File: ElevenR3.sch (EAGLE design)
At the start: 63 parts, among them IC1 ATMEGA328P, IC2 ATMEGA8U2-MU, IC3 MC33269DT-5.0, IC4 LM358D, IC5 LP2985-33DBVR, J2 Analog, J3 Digital_8_13, J4 Digital_0_7, J5 DC_2_1MM, J6 Digital_0_7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

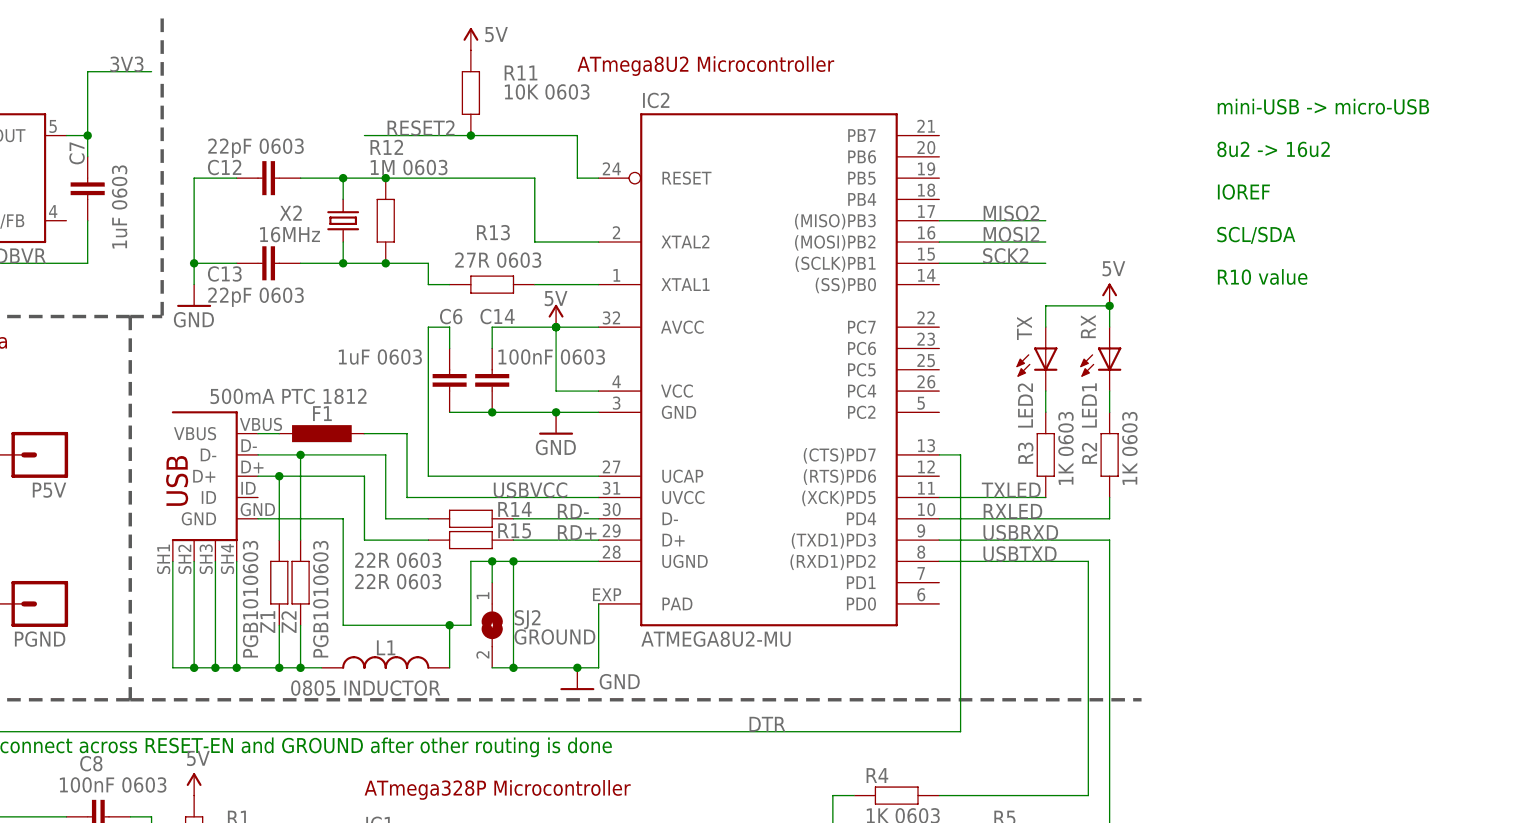
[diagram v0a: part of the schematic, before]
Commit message: Routed I2C and converted to microUSB
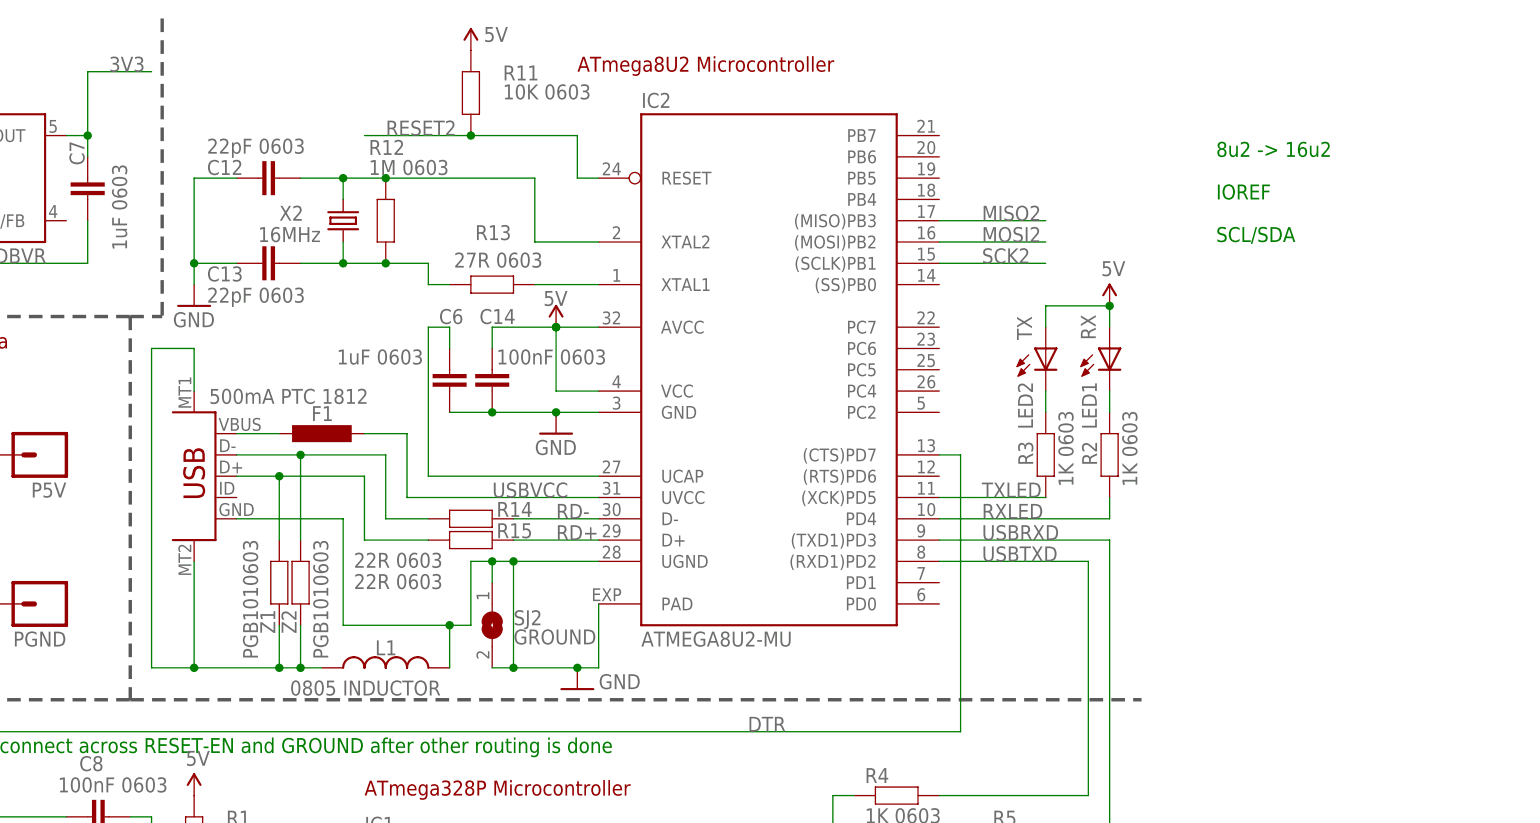
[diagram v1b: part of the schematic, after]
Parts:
- removed P1: USB-FT, freetronics-master-v1:USB-FT
- added X3: USBSF-MICROB, freetronics-jon:USBSF-MICROB
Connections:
- net GND: now also X3.GND; no longer P1.GND
- net N$115: now also X3.VBUS; no longer P1.VBUS
- net N$16: now also X3.D+; no longer P1.D+
- net N$17: now also X3.D-; no longer P1.D-
- net N$3: now also X3.MT1, X3.MT2; no longer P1.SH$1, P1.SH$2, P1.SH$3, P1.SH$4
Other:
- note removed: "R10 value"
- note removed: "mini-USB -> micro-USB"
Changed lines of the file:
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@@
 <layer number="101" name="Patch_Top" color="12" fill="4" visible="yes" active="yes"/>
 <layer number="102" name="Vscore" color="7" fill="1" visible="yes" active="yes"/>
+<layer number="103" name="fp3" color="7" fill="1" visible="yes" active="yes"/>
 <layer number="104" name="Name" color="7" fill="1" visible="yes" active="yes"/>
+<layer number="105" name="Beschreib" color="9" fill="1" visible="yes" active="yes"/>
+<layer number="106" name="BGA-Top" color="4" fill="1" visible="yes" active="yes"/>
+<layer number="107" name="BD-Top" color="5" fill="1" visible="yes" active="yes"/>
+<layer number="108" name="fp8" color="7" fill="1" visible="yes" active="yes"/>
+<layer number="109" name="fp9" color="7" fill="1" visible="yes" active="yes"/>
+<layer number="110" name="fp0" color="7" fill="1" visible="yes" active="yes"/>
+<layer number="111" name="LPC17xx" color="7" fill="1" visible="yes" active="yes"/>
+<layer number="112" name="tSilk" color="7" fill="1" visible="yes" active="yes"/>
 <layer number="116" name="Patch_BOT" color="9" fill="4" visible="yes" active="yes"/>
 <layer number="121" name="_tsilk" color="7" fill="1" visible="yes" active="yes"/>
 <layer number="122" name="_bsilk" color="7" fill="1" visible="yes" active="yes"/>
+<layer number="123" name="tTestmark" color="7" fill="1" visible="yes" active="yes"/>
+<layer number="124" name="bTestmark" color="7" fill="1" visible="yes" active="yes"/>
+<layer number="125" name="_tNames" color="7" fill="1" visible="yes" active="yes"/>
+<layer number="126" name="_bNames" color="7" fill="1" visible="yes" active="yes"/>
+<layer number="127" name="_tValues" color="7" fill="1" visible="yes" active="yes"/>
+<layer number="128" name="_bValues" color="7" fill="1" visible="yes" active="yes"/>
+<layer number="131" name="tAdjust" color="7" fill="1" visible="yes" active="yes"/>
+<layer number="132" name="bAdjust" color="7" fill="1" visible="yes" active="yes"/>
+<layer number="144" name="Drill_legend" color="7" fill="1" visible="yes" active="yes"/>
 <layer number="151" name="HeatSink" color="7" fill="1" visible="yes" active="yes"/>
+<layer number="152" name="_bDocu" color="7" fill="1" visible="yes" active="yes"/>
+<layer number="199" name="Contour" color="7" fill="1" visible="yes" active="yes"/>
 <layer number="200" name="200bmp" color="1" fill="10" visible="no" active="no"/>
 <layer number="201" name="201bmp" color="2" fill="1" visible="no" active="no"/>
@@
 <layer number="223" name="223bmp" color="7" fill="1" visible="yes" active="yes"/>
 <layer number="224" name="224bmp" color="7" fill="1" visible="yes" active="yes"/>
+<layer number="231" name="Eagle3D_PG1" color="7" fill="1" visible="yes" active="yes"/>
+<layer number="232" name="Eagle3D_PG2" color="7" fill="1" visible="yes" active="yes"/>
+<layer number="233" name="Eagle3D_PG3" color="7" fill="1" visible="yes" active="yes"/>
+<layer number="248" name="Housing" color="7" fill="1" visible="yes" active="yes"/>
+<layer number="249" name="Edge" color="7" fill="1" visible="yes" active="yes"/>
 <layer number="250" name="Descript" color="3" fill="1" visible="no" active="no"/>
 <layer number="251" name="SMDround" color="12" fill="11" visible="no" active="no"/>
@@
 <part name="L1" library="freetronics-master-v1" deviceset="INDUCTOR" device="0805-LARGE" value="0805 INDUCTOR"/>
 <part name="C6" library="freetronics" deviceset="CAP" device="0603" value="1uF 0603"/>
-<part name="P1" library="freetronics-master-v1" deviceset="USB-FT" device=""/>
 <part name="GND1" library="SparkFun" deviceset="GND" device=""/>
 <part name="GND6" library="SparkFun" deviceset="GND" device=""/>
 <part name="J6" library="freetronics" deviceset="M08" device="" value="Digital_0_7"/>
+<part name="X3" library="freetronics-jon" deviceset="USBSF" device="-MICROB"/>
 </parts>
 <sheets>
@@
 <frame x1="210.82" y1="5.08" x2="243.84" y2="10.16" columns="8" rows="5" layer="94"/>
 <frame x1="88.9" y1="101.6" x2="121.92" y2="139.7" columns="0" rows="0" layer="94"/>
-<text x="254" y="170.18" size="1.778" layer="91">mini-USB -&gt; micro-USB</text>
 <text x="254" y="165.1" size="1.778" layer="91">8u2 -&gt; 16u2</text>
 <text x="254" y="160.02" size="1.778" layer="91">IOREF</text>
 <text x="254" y="154.94" size="1.778" layer="91">SCL/SDA</text>
-<text x="254" y="149.86" size="1.778" layer="91">R10 value</text>
 </plain>
 <instances>
@@
 <attribute name="VALUE" x="149.098" y="140.335" size="1.778" layer="96"/>
 </instance>
-<instance part="P1" gate="G$1" x="127" y="121.92"/>
 <instance part="GND1" gate="1" x="175.26" y="132.08"/>
 <instance part="GND6" gate="1" x="177.8" y="101.6" smashed="yes">
@@
 <attribute name="VALUE" x="8.128" y="31.75" size="1.778" layer="96" rot="MR180"/>
 </instance>
+<instance part="X3" gate="G$1" x="132.08" y="127" rot="R180"/>
 </instances>
 <busses>
@@
 <wire x1="170.18" y1="104.14" x2="177.8" y2="104.14" width="0.1524" layer="91"/>
 <wire x1="170.18" y1="104.14" x2="170.18" y2="116.84" width="0.1524" layer="91"/>
-<wire x1="139.7" y1="121.92" x2="149.86" y2="121.92" width="0.1524" layer="91"/>
+<wire x1="137.16" y1="121.92" x2="149.86" y2="121.92" width="0.1524" layer="91"/>
 <wire x1="149.86" y1="121.92" x2="149.86" y2="109.22" width="0.1524" layer="91"/>
 <wire x1="149.86" y1="109.22" x2="162.56" y2="109.22" width="0.1524" layer="91"/>
@@
 <pinref part="GND6" gate="1" pin="GND"/>
 <pinref part="SJ2" gate="1" pin="2"/>
-<pinref part="P1" gate="G$1" pin="GND"/>
 <pinref part="L1" gate="G$1" pin="2"/>
 <pinref part="IC2" gate="G$1" pin="UGND"/>
 <pinref part="SJ2" gate="1" pin="1"/>
+<pinref part="X3" gate="G$1" pin="GND"/>
 </segment>
 </net>
@@
 <net name="N$3" class="0">
 <segment>
-<wire x1="129.54" y1="116.84" x2="129.54" y2="104.14" width="0.1524" layer="91"/>
-<wire x1="129.54" y1="104.14" x2="132.08" y2="104.14" width="0.1524" layer="91"/>
-<wire x1="132.08" y1="104.14" x2="134.62" y2="104.14" width="0.1524" layer="91"/>
-<wire x1="134.62" y1="104.14" x2="137.16" y2="104.14" width="0.1524" layer="91"/>
-<wire x1="137.16" y1="104.14" x2="142.24" y2="104.14" width="0.1524" layer="91"/>
 <wire x1="142.24" y1="104.14" x2="144.78" y2="104.14" width="0.1524" layer="91"/>
-<wire x1="132.08" y1="116.84" x2="132.08" y2="104.14" width="0.1524" layer="91"/>
-<wire x1="134.62" y1="116.84" x2="134.62" y2="104.14" width="0.1524" layer="91"/>
-<wire x1="137.16" y1="116.84" x2="137.16" y2="104.14" width="0.1524" layer="91"/>
 <wire x1="142.24" y1="109.22" x2="142.24" y2="104.14" width="0.1524" layer="91"/>
 <wire x1="144.78" y1="109.22" x2="144.78" y2="104.14" width="0.1524" layer="91"/>
 <wire x1="144.78" y1="104.14" x2="147.32" y2="104.14" width="0.1524" layer="91"/>
-<junction x="132.08" y="104.14"/>
-<junction x="134.62" y="104.14"/>
-<junction x="137.16" y="104.14"/>
 <junction x="142.24" y="104.14"/>
 <junction x="144.78" y="104.14"/>
-<pinref part="P1" gate="G$1" pin="SH$1"/>
-<pinref part="P1" gate="G$1" pin="SH$2"/>
-<pinref part="P1" gate="G$1" pin="SH$3"/>
-<pinref part="P1" gate="G$1" pin="SH$4"/>
 <pinref part="Z1" gate="G$1" pin="2"/>
 <pinref part="Z2" gate="G$1" pin="2"/>
 <pinref part="L1" gate="G$1" pin="1"/>
+<pinref part="X3" gate="G$1" pin="MT2"/>
+<wire x1="132.08" y1="116.84" x2="132.08" y2="104.14" width="0.1524" layer="91"/>
+<wire x1="132.08" y1="104.14" x2="142.24" y2="104.14" width="0.1524" layer="91"/>
+<pinref part="X3" gate="G$1" pin="MT1"/>
+<wire x1="132.08" y1="137.16" x2="132.08" y2="142.24" width="0.1524" layer="91"/>
+<wire x1="132.08" y1="142.24" x2="127" y2="142.24" width="0.1524" layer="91"/>
+<wire x1="127" y1="142.24" x2="127" y2="104.14" width="0.1524" layer="91"/>
+<wire x1="127" y1="104.14" x2="132.08" y2="104.14" width="0.1524" layer="91"/>
+<junction x="132.08" y="104.14"/>
 </segment>
 </net>
@@
 <segment>
 <wire x1="142.24" y1="119.38" x2="142.24" y2="127" width="0.1524" layer="91"/>
-<wire x1="142.24" y1="127" x2="139.7" y2="127" width="0.1524" layer="91"/>
 <wire x1="142.24" y1="127" x2="152.4" y2="127" width="0.1524" layer="91"/>
 <wire x1="152.4" y1="127" x2="152.4" y2="119.38" width="0.1524" layer="91"/>
@@
 <junction x="142.24" y="127"/>
 <pinref part="Z1" gate="G$1" pin="1"/>
-<pinref part="P1" gate="G$1" pin="D+"/>
 <pinref part="R15" gate="G$1" pin="2"/>
+<pinref part="X3" gate="G$1" pin="D+"/>
+<wire x1="142.24" y1="127" x2="137.16" y2="127" width="0.1524" layer="91"/>
 </segment>
 </net>
@@
 <segment>
 <wire x1="144.78" y1="119.38" x2="144.78" y2="129.54" width="0.1524" layer="91"/>
-<wire x1="144.78" y1="129.54" x2="139.7" y2="129.54" width="0.1524" layer="91"/>
 <wire x1="160.02" y1="121.92" x2="154.94" y2="121.92" width="0.1524" layer="91"/>
 <wire x1="154.94" y1="121.92" x2="154.94" y2="129.54" width="0.1524" layer="91"/>
@@
 <junction x="144.78" y="129.54"/>
 <pinref part="Z2" gate="G$1" pin="1"/>
-<pinref part="P1" gate="G$1" pin="D-"/>
 <pinref part="R14" gate="G$1" pin="2"/>
+<pinref part="X3" gate="G$1" pin="D-"/>
+<wire x1="137.16" y1="129.54" x2="144.78" y2="129.54" width="0.1524" layer="91"/>
 </segment>
 </net>
 <net name="N$115" class="0">
 <segment>
-<wire x1="142.24" y1="132.08" x2="139.7" y2="132.08" width="0.1524" layer="91"/>
 <pinref part="F1" gate="G$1" pin="1"/>
-<pinref part="P1" gate="G$1" pin="VBUS"/>
-</segment>
-</net>
+<pinref part="X3" gate="G$1" pin="VBUS"/>
+<wire x1="142.24" y1="132.08" x2="137.16" y2="132.08" width="0.1524" layer="91"/>
+</segment>
+</net>

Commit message: Overlay, layout, and schematic tweaks
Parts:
- IC2: value ATMEGA8U2-MU -> ATMEGA16U2-MU
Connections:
- new net N$1: C8.1, SJ1.2
- new net N$116: IC2.UGND, L1.2, SJ2.1, X3.GND
- net DTR: no longer C8.1, SJ1.2
- net GND: no longer IC2.UGND, L1.2, SJ2.1, X3.GND
- net N$3: now also X3.FIX1, X3.FIX2, X3.TAB1, X3.TAB2; no longer X3.MT1, X3.MT2
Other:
- note added: "(C)2012 Freetronics Pty Ltd: www.freetronics.com"
- note added: "(Linked)"
- note added: "Freetronics "Eleven" R3"
- note added: "Released under the TAPR Open Hardware License: www.tapr.org/ohl"
- note added: "V3.0 (2012-07-02)"
- note added: "www.freetronics.com/eleven"
- note removed: "8u2 -> 16u2"
- note removed: "Arduino Compatible Board"
- note removed: "Freetronics Eleven"
- note removed: "Version 1.0"
- note removed: "www.freetronics.com"
- moved on the sheet: C11, IC1, IC4A, IC4B, LED3, P5V, PGND, Q1, Q2, R4, R5, R7

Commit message: Clearances
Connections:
- net N$116 renamed UGND
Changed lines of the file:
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@@
 </segment>
 </net>
-<net name="N$116" class="0">
+<net name="UGND" class="0">
 <segment>
 <wire x1="137.16" y1="121.92" x2="149.86" y2="121.92" width="0.1524" layer="91"/>
@@
 </sheet>
 </sheets>
+<errors>
+</errors>
 </schematic>
 </drawing>
